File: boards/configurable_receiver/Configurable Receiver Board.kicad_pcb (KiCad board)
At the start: 4 copper layers, 42.5 x 38.5 mm, 22 parts, among them J1 NeoPixel, J2 NeoPixel, J3 NeoPixel, J4 NeoPixel, J5 Sensor, P4 SERIAL, SW1 Switch_SPDT_x2, SW2 Switch_DPST, U0 10118194, U1 LM3671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

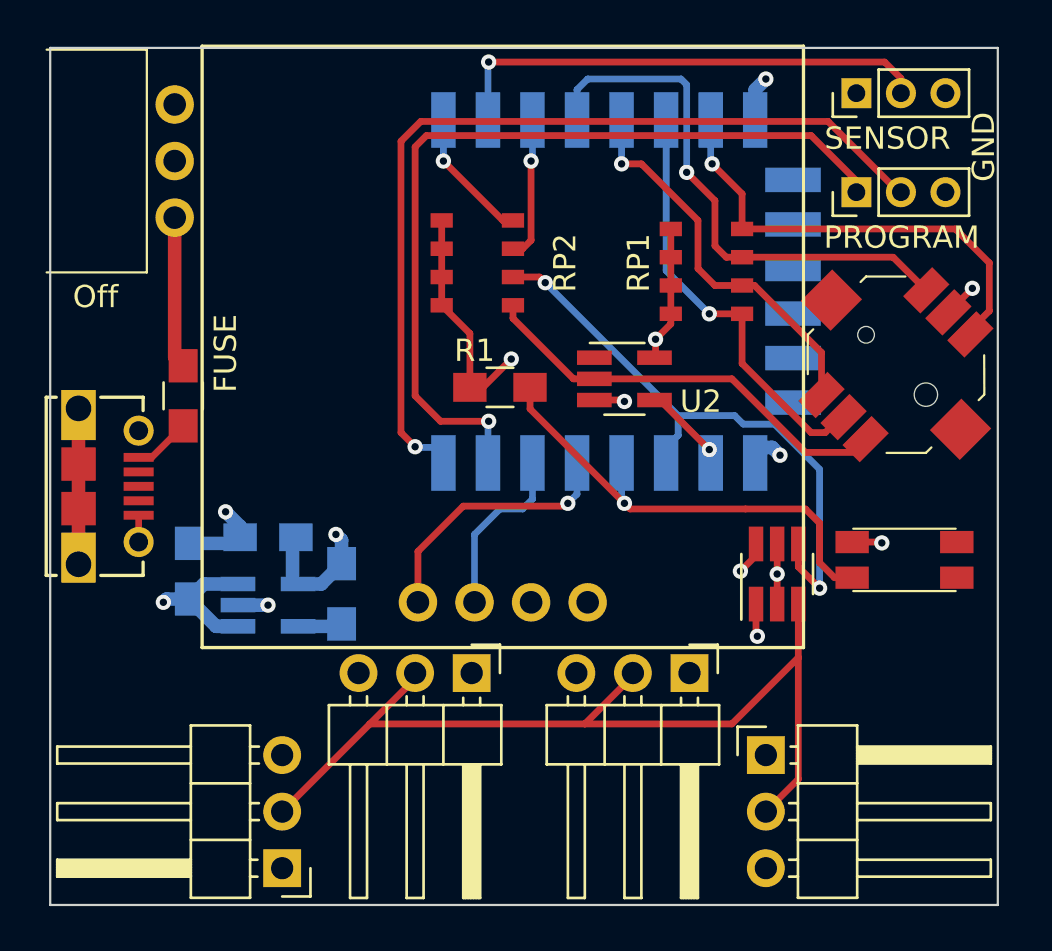
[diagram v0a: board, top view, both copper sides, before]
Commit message: Created v4 of the receiver
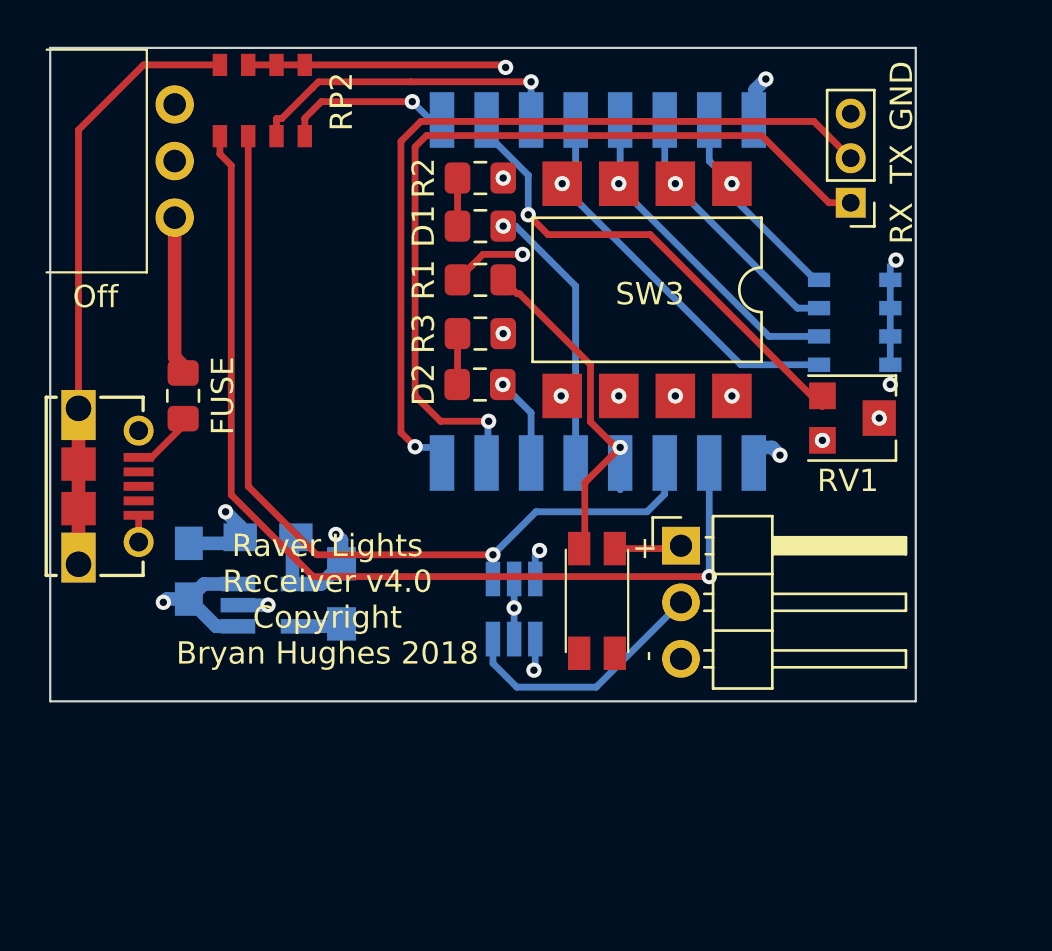
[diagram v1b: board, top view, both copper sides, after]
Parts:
- removed J1, J2, J3: NeoPixel, Pin_Headers:Pin_Header_Angled_1x03_Pitch2.54mm
- removed J5: Sensor, Pin_Headers:Pin_Header_Straight_1x03_Pitch2.00mm
- removed U2: 74AUP1G14, TO_SOT_Packages_SMD:SOT-23-5_HandSoldering
- removed U4: DIY-OLED-0.96, nebrius-lcd:DIY-OLED-0.96
- removed U5: SF303GJ26, nebrius-switch:SF303GJ26
- added D1: LED, Resistor_SMD:R_0805_2012Metric_Pad1.15x1.40mm_HandSolder, F.Cu at (113.2, 111.2)
- added D2: LED, Resistor_SMD:R_0805_2012Metric_Pad1.15x1.40mm_HandSolder, F.Cu at (113.2, 118.3)
- added R2: 68, Resistor_SMD:R_0805_2012Metric_Pad1.15x1.40mm_HandSolder, F.Cu at (113.2, 109.0)
- added R3: 68, Resistor_SMD:R_0805_2012Metric_Pad1.15x1.40mm_HandSolder, F.Cu at (113.2, 116.0)
- added RV1: R_POT, nebrius-switch:TC33-potentiometer, F.Cu at (128.6, 119.8)
- added SW3: SW_DIP_x04, Package_DIP:SMDIP-8_W9.53mm, F.Cu at (120.7, 114.0)
- F0, R1: footprint Resistors_SMD:R_0805_HandSoldering -> Resistor_SMD:R_0805_2012Metric_Pad1.15x1.40mm_HandSolder
- RP1, U7: moved to B.Cu
- SW1: footprint CL-SA-12C:CL-SA-12C4 -> nebrius-switch:CL-SA-12C4
- U3: value ESP-12E -> ESP-12F; footprint ESP8266:ESP-12E_SMD -> ESP8266:ESP-12F_SMD
- moved SW2 13.9 mm to (118.5, 128.0), turned to 90 degrees
- moved RP2 12.1 mm to (103.4, 105.5), turned to 0 degrees
- moved U7 11.9 mm to (114.7, 128.4)
- moved RP1 7.04 mm to (130.0, 115.5)
- moved J4 5.73 mm to (122.2, 125.5), turned to 0 degrees
- moved R1 4.91 mm to (113.2, 113.6)
- moved P4 0.54 mm to (129.9, 110.1), turned to 180 degrees
- moved U3 0.06 mm to (111.5, 107.1)
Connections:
- RP1 pad 5: VCC -> GND
- RP1 pad 6: VCC -> GND
- RP1 pad 7: VCC -> GND
- RP1 pad 8: VCC -> GND
- RP2 pad 8: VCC -> GND
- SW1 pad 1: (no net) -> Net-(SW1-Pad1)
- SW2 pad 1: (no net) -> Net-(SW2-Pad1)
- SW2 pad 2: (no net) -> Net-(SW2-Pad2)
- U0 pad 2: (no net) -> Net-(U0-Pad2)
- U0 pad 3: (no net) -> Net-(U0-Pad3)
- U0 pad 4: (no net) -> Net-(U0-Pad4)
- U3 pad 10: Net-(U2-Pad4) -> Net-(RP2-Pad1)
- U3 pad 4: Net-(RP1-Pad3) -> Net-(RP1-Pad1)
- U3 pad 6: Net-(RP1-Pad1) -> Net-(RP1-Pad3)
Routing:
- net Net-(J4-Pad2): track 42.3 -> 11.6 mm
- net Net-(RP2-Pad1): track 19.3 -> 45.1 mm, vias 0 -> 1
- net GND: track 21.3 -> 44.7 mm, vias 7 -> 8
- net Net-(RP1-Pad3): track 25.7 -> 11.2 mm
- net Net-(RP2-Pad2): track 26.7 -> 40.0 mm, vias 2 -> 1
- net Net-(RP1-Pad4): track 20.1 -> 8.62 mm
- net Net-(RP2-Pad3): track 5.70 -> 15.3 mm
- net Net-(D2-Pad2): track 8.63 -> 3.35 mm, vias 0 -> 1
- net Net-(R1-Pad2): track 22.2 -> 17.0 mm
- net Net-(U2-Pad4): track 3.50 -> 0.00 mm, vias 1 -> 0
- net Net-(P4-Pad2): track 39.4 -> 36.5 mm
- net Net-(RP1-Pad2): track 16.9 -> 14.1 mm
- net Net-(RP2-Pad4): track 5.37 -> 8.02 mm
- net Net-(D2-Pad1): track 0.00 -> 2.29 mm
- net Net-(D1-Pad1): track 0.00 -> 2.16 mm
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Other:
- board size 42.5 x 38.5 mm -> 38.9 x 29.3 mm
- board text added: "+"
- board text added: "-"
- board text added: "RX"
- board text added: "Raver Lights Receiver v4.0 Copyright Bryan Hughes 2018"
- board text added: "TX"
- board text removed: "PROGRAM"
- board text removed: "Raver Lights Hub v3.3 Copyright Bryan Hughes 2018"
- board text removed: "SENSOR"
